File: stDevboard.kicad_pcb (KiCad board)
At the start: 4 copper layers, 50 x 100 mm, 142 parts, among them IC1 MPM3610GQV-Z, IC2 IRFR9014PBF, IC3 ICM-45686, IC4 ICM-45686, IC5 MMC5983MA, IC6 AT25SF041B-SSHB-B, J1 battery, J10 73412-0114, J11 USB_C_Receptacle_USB2.0_16P, J12 73412-0114, J13 Conn_01x04, J14 Micro_SD_Card_Det2, J2 USB_C_Receptacle_USB2.0_16P, J3 Conn_02x03_Top_Bottom, J4 Screw_Terminal_01x02, J5 Screw_Terminal_01x02, J6 Screw_Terminal_01x02, J7 Screw_Terminal_01x02, J8 Screw_Terminal_01x02, J9 Screw_Terminal_01x02, Q1 IRLML6244, Q2 IRLML6244, Q3 IRLML6244, Q4 IRLML6244, Q5 IRLML6244, Q6 IRLML6244, U1 STM32U073CCUx, U2 STM32U585CIUxQ, U3 BMP581, U4 MAX-M10S, Y1 ECS-160-8-36B2-CKM-TR, Y2 CM7V-T1A-32.768KHZ, Y3 ECS-TXO-25CSMV-320-AM-TR, Y4 CM7V-T1A-32.768KHZ

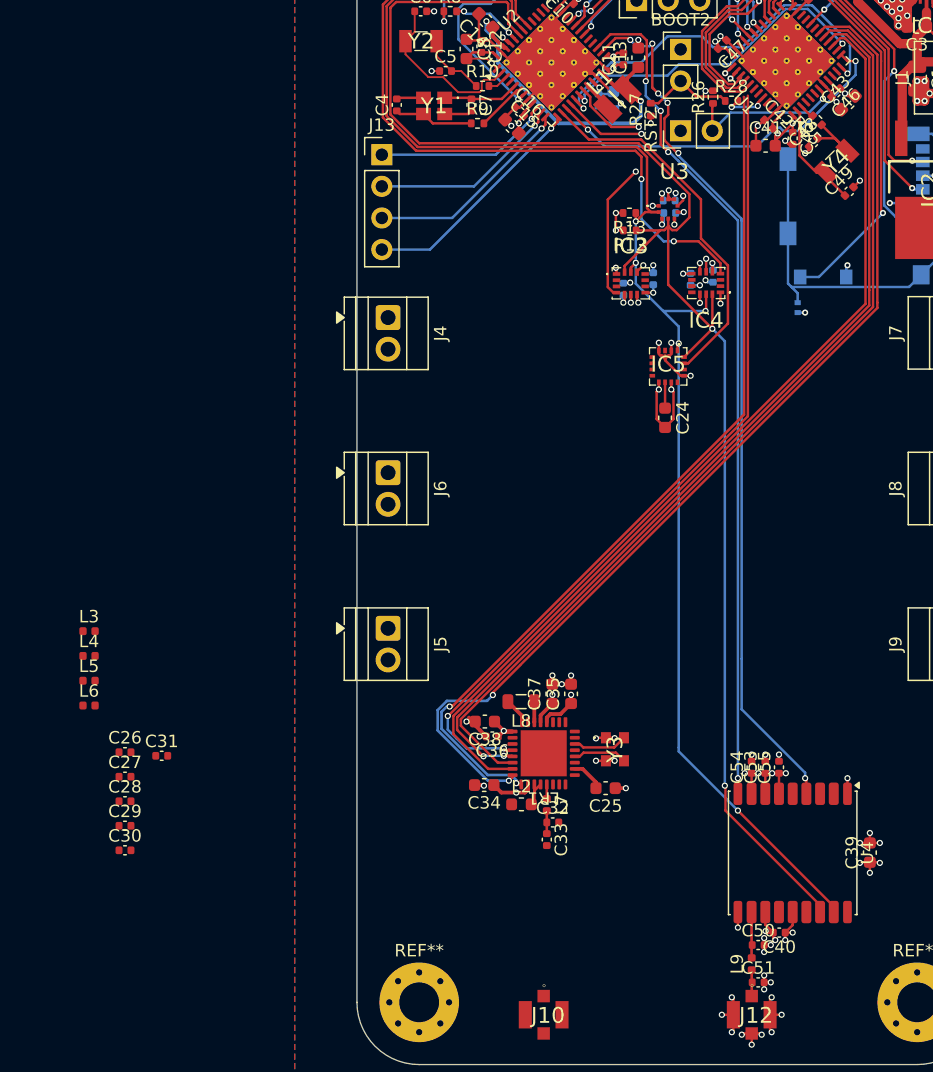
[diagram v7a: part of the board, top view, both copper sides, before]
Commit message: added piezo buzzer, rf hopefully finished! just need to send to mpk for check now
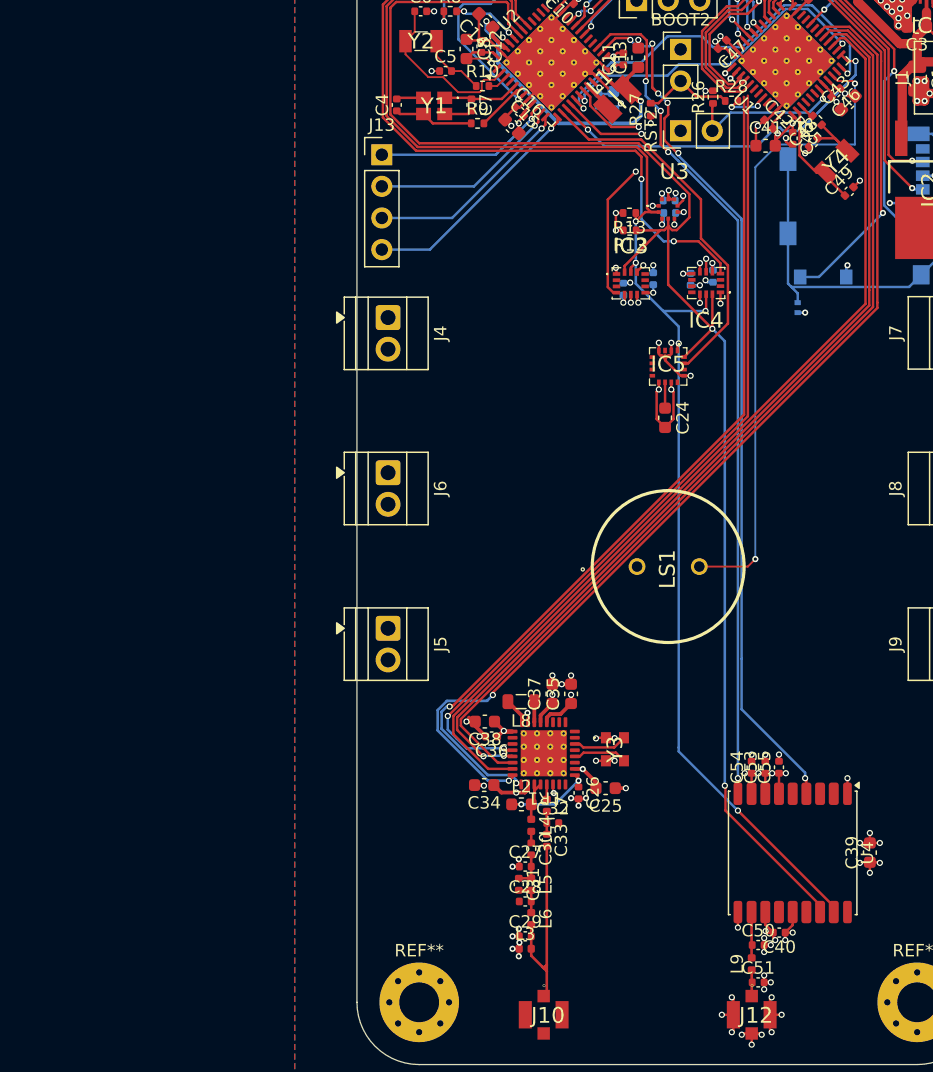
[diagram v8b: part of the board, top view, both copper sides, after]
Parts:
- added LS1: PS1240P02BT, footprints:PS1240P02BT, F.Cu at (125.0, 135.0)
- moved L3 43.3 mm to (113.5, 165.7)
- moved L6 39.4 mm to (114.0, 163.3), turned to -90 degrees
- moved L5 39.1 mm to (114.0, 160.5), turned to -90 degrees
- moved L4 38.0 mm to (114.0, 155.8), turned to -90 degrees
- moved C26 36.6 mm to (117.8, 153.2), turned to -90 degrees
- moved C29 33.4 mm to (113.5, 164.7)
- moved C28 33.1 mm to (113.5, 161.9)
- moved C27 33.0 mm to (113.5, 159.1)
- moved C30 32.6 mm to (114.0, 157.7), turned to -90 degrees
- moved C31 30.5 mm to (113.0, 160.5), turned to -90 degrees
- moved C36 0.05 mm to (110.8, 148.7)
- moved L7 0.05 mm to (115.2, 154.2)
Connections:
- U1 pad 10: unconnected-(U1-PA0-Pad10) -> Net-(U1-PA0)
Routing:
- net Net-(U1-PA0): track 0.00 -> 52.0 mm, vias 0 -> 2
- net Net-(J10-SIGNAL): track 0.00 -> 17.0 mm
- net GND: track 183.5 -> 191.4 mm, vias 115 -> 127
- net vr_pa: track 0.00 -> 7.24 mm, vias 0 -> 2
- net Net-(C27-Pad2): track 0.00 -> 2.87 mm
- net Net-(C28-Pad2): track 0.00 -> 2.80 mm
- net Net-(LR1-RFO_LF1): track 2.41 -> 3.61 mm
- net Net-(C30-Pad1): track 0.00 -> 0.93 mm
- net +3.3V: track 107.2 -> 107.3 mm, vias 57 -> 58
